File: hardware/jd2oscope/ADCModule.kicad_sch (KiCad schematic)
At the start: 2 parts, among them J1 5227161-2, U1 ADS7279IPW

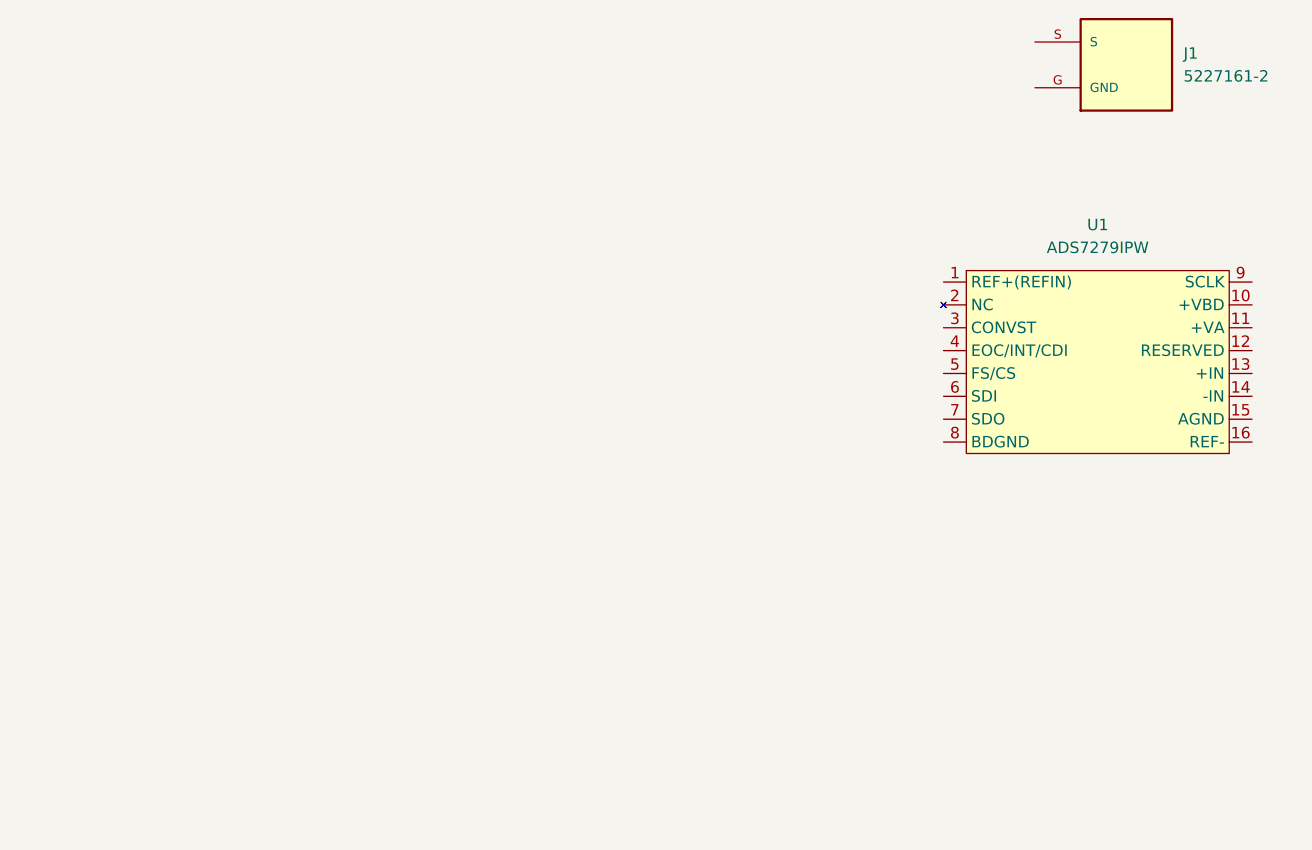
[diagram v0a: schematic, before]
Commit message: feat: opAmpCircuit cleanup
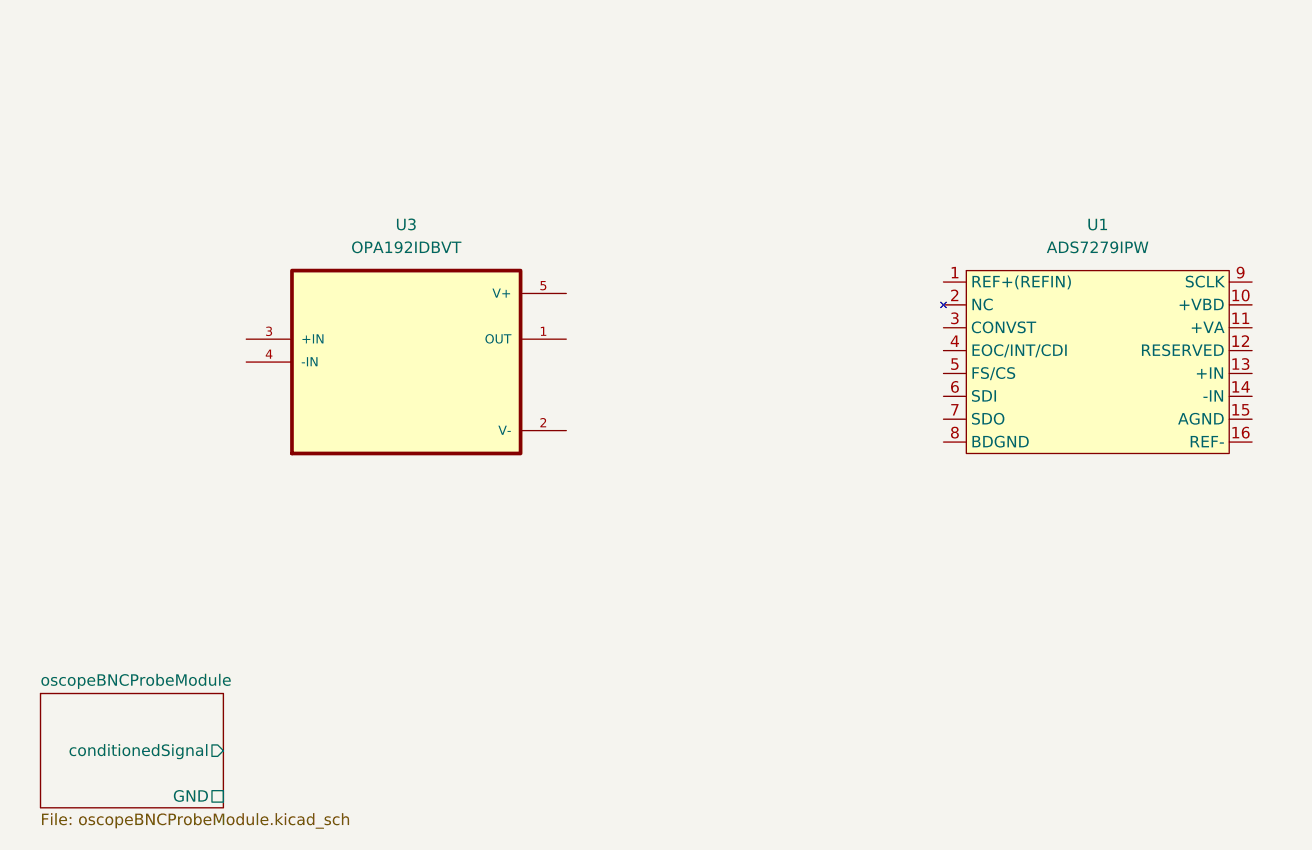
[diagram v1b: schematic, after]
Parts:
- removed J1: 5227161-2, 5227161-2:TE_5227161-2, symbol BNCFemaleConn:5227161-2
- added U3: OPA192IDBVT, OPA192IDBVT:SOT95P280X145-5N, symbol opAmp:OPA192IDBVT
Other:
- added sheet oscopeBNCProbeModule (oscopeBNCProbeModule.kicad_sch)
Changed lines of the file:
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@@
 	)
 	(symbol
-		(lib_id "BNCFemaleConn:5227161-2")
-		(at 158.75 59.69 0)
+		(lib_id "opAmp:OPA192IDBVT")
+		(at 78.74 92.71 0)
 		(unit 1)
 		(exclude_from_sim no)
@@
 		(dnp no)
 		(fields_autoplaced yes)
-		(property "Reference" "J1"
-			(at 165.1 58.4199 0)
-			(effects
-				(font
-					(size 1.27 1.27)
-				)
-				(justify left)
-			)
-		)
-		(property "Value" "5227161-2"
-			(at 165.1 60.9599 0)
-			(effects
-				(font
-					(size 1.27 1.27)
-				)
-				(justify left)
-			)
-		)
-		(property "Footprint" "5227161-2:TE_5227161-2"
-			(at 158.75 59.69 0)
+		(property "Reference" "U3"
+			(at 78.74 77.47 0)
+			(effects
+				(font
+					(size 1.27 1.27)
+				)
+			)
+		)
+		(property "Value" "OPA192IDBVT"
+			(at 78.74 80.01 0)
+			(effects
+				(font
+					(size 1.27 1.27)
+				)
+			)
+		)
+		(property "Footprint" "OPA192IDBVT:SOT95P280X145-5N"
+			(at 78.74 92.71 0)
 			(effects
 				(font
@@
 		)
 		(property "Datasheet" ""
-			(at 158.75 59.69 0)
+			(at 78.74 92.71 0)
 			(effects
 				(font
@@
 		)
 		(property "Description" ""
-			(at 158.75 59.69 0)
-			(effects
-				(font
-					(size 1.27 1.27)
-				)
-				(hide yes)
-			)
-		)
-		(property "Comment" "5227161-2"
-			(at 158.75 59.69 0)
-			(effects
-				(font
-					(size 1.27 1.27)
-				)
-				(justify bottom)
-				(hide yes)
-			)
-		)
-		(property "MF" "TE Connectivity"
-			(at 158.75 59.69 0)
-			(effects
-				(font
-					(size 1.27 1.27)
-				)
-				(justify bottom)
-				(hide yes)
-			)
-		)
-		(property "MAXIMUM_PACKAGE_HEIGHT" "16.13 mm"
-			(at 158.75 59.69 0)
-			(effects
-				(font
-					(size 1.27 1.27)
-				)
-				(justify bottom)
-				(hide yes)
-			)
-		)
-		(property "Package" "None"
-			(at 158.75 59.69 0)
+			(at 78.74 92.71 0)
+			(effects
+				(font
+					(size 1.27 1.27)
+				)
+				(hide yes)
+			)
+		)
+		(property "MF" "Texas Instruments"
+			(at 78.74 92.71 0)
+			(effects
+				(font
+					(size 1.27 1.27)
+				)
+				(justify bottom)
+				(hide yes)
+			)
+		)
+		(property "Description_1" "\n                        \n                            High-Voltage, Rail-to-Rail Input/Output, 5µV, 0.2µV/˚C, Precision Operational Amplifier\n                        \n"
+			(at 78.74 92.71 0)
+			(effects
+				(font
+					(size 1.27 1.27)
+				)
+				(justify bottom)
+				(hide yes)
+			)
+		)
+		(property "Package" "SOT-23-5 Texas Instruments"
+			(at 78.74 92.71 0)
 			(effects
 				(font
@@
 		)
 		(property "Price" "None"
-			(at 158.75 59.69 0)
-			(effects
-				(font
-					(size 1.27 1.27)
-				)
-				(justify bottom)
-				(hide yes)
-			)
-		)
-		(property "Check_prices" "https://www.snapeda.com/parts/5227161-2/TE+Connectivity/view-part/?ref=eda"
-			(at 158.75 59.69 0)
-			(effects
-				(font
-					(size 1.27 1.27)
-				)
-				(justify bottom)
-				(hide yes)
-			)
-		)
-		(property "STANDARD" "Manufacturer Recommendations"
-			(at 158.75 59.69 0)
-			(effects
-				(font
-					(size 1.27 1.27)
-				)
-				(justify bottom)
-				(hide yes)
-			)
-		)
-		(property "PARTREV" "B3"
-			(at 158.75 59.69 0)
-			(effects
-				(font
-					(size 1.27 1.27)
-				)
-				(justify bottom)
-				(hide yes)
-			)
-		)
-		(property "SnapEDA_Link" "https://www.snapeda.com/parts/5227161-2/TE+Connectivity/view-part/?ref=snap"
-			(at 158.75 59.69 0)
-			(effects
-				(font
-					(size 1.27 1.27)
-				)
-				(justify bottom)
-				(hide yes)
-			)
-		)
-		(property "MP" "5227161-2"
-			(at 158.75 59.69 0)
-			(effects
-				(font
-					(size 1.27 1.27)
-				)
-				(justify bottom)
-				(hide yes)
-			)
-		)
-		(property "EU_RoHS_Compliance" "Compliant with Exemptions"
-			(at 158.75 59.69 0)
-			(effects
-				(font
-					(size 1.27 1.27)
-				)
-				(justify bottom)
-				(hide yes)
-			)
-		)
-		(property "Description_1" "\n                        \n                            CONNECTOR, RF, BNC, JACK, PCB, RIGHT ANGLE, WITH PINS | TE Connectivity 5227161-2\n                        \n"
-			(at 158.75 59.69 0)
-			(effects
-				(font
-					(size 1.27 1.27)
-				)
-				(justify bottom)
-				(hide yes)
-			)
-		)
-		(property "Number_of_Positions" "1"
-			(at 158.75 59.69 0)
+			(at 78.74 92.71 0)
+			(effects
+				(font
+					(size 1.27 1.27)
+				)
+				(justify bottom)
+				(hide yes)
+			)
+		)
+		(property "SnapEDA_Link" "https://www.snapeda.com/parts/OPA192IDBVT/Texas+Instruments/view-part/?ref=snap"
+			(at 78.74 92.71 0)
+			(effects
+				(font
+					(size 1.27 1.27)
+				)
+				(justify bottom)
+				(hide yes)
+			)
+		)
+		(property "MP" "OPA192IDBVT"
+			(at 78.74 92.71 0)
 			(effects
 				(font
@@
 		)
 		(property "Availability" "In Stock"
-			(at 158.75 59.69 0)
-			(effects
-				(font
-					(size 1.27 1.27)
-				)
-				(justify bottom)
-				(hide yes)
-			)
-		)
-		(property "MANUFACTURER" "TE Connectivity"
-			(at 158.75 59.69 0)
-			(effects
-				(font
-					(size 1.27 1.27)
-				)
-				(justify bottom)
-				(hide yes)
-			)
-		)
-		(pin "S"
-		)
-		(pin "G"
+			(at 78.74 92.71 0)
+			(effects
+				(font
+					(size 1.27 1.27)
+				)
+				(justify bottom)
+				(hide yes)
+			)
+		)
+		(property "Check_prices" "https://www.snapeda.com/parts/OPA192IDBVT/Texas+Instruments/view-part/?ref=eda"
+			(at 78.74 92.71 0)
+			(effects
+				(font
+					(size 1.27 1.27)
+				)
+				(justify bottom)
+				(hide yes)
+			)
+		)
+		(pin "4"
+		)
+		(pin "5"
+		)
+		(pin "3"
+		)
+		(pin "2"
+		)
+		(pin "1"
+		)
+		(instances
+			(project ""
+				(path "/eb18a3da-9fbf-4329-a814-1afab785c817/a55cf82a-acda-4de6-8ce7-2cf91fdca590"
+					(reference "U3")
+					(unit 1)
+				)
+			)
+		)
+	)
+	(sheet
+		(at 38.1 129.54)
+		(size 20.32 12.7)
+		(fields_autoplaced yes)
+		(stroke
+			(width 0.1524)
+			(type solid)
+		)
+		(fill
+			(color 0 0 0 0.0000)
+		)
+		(property "Sheetname" "oscopeBNCProbeModule"
+			(at 38.1 128.8284 0)
+			(effects
+				(font
+					(size 1.27 1.27)
+				)
+				(justify left bottom)
+			)
+		)
+		(property "Sheetfile" "oscopeBNCProbeModule.kicad_sch"
+			(at 38.1 142.8246 0)
+			(effects
+				(font
+					(size 1.27 1.27)
+				)
+				(justify left top)
+			)
+		)
+		(pin "GND" passive
+			(at 58.42 140.97 0)
+			(effects
+				(font
+					(size 1.27 1.27)
+				)
+				(justify right)
+			)
+		)
+		(pin "conditionedSignal" output
+			(at 58.42 135.89 0)
+			(effects
+				(font
+					(size 1.27 1.27)
+				)
+				(justify right)
+			)
 		)
 		(instances
 			(project "jd2oscope"
 				(path "/eb18a3da-9fbf-4329-a814-1afab785c817/a55cf82a-acda-4de6-8ce7-2cf91fdca590"
-					(reference "J1")
-					(unit 1)
-				)
-			)
+					(page "2")
+				)
+			)

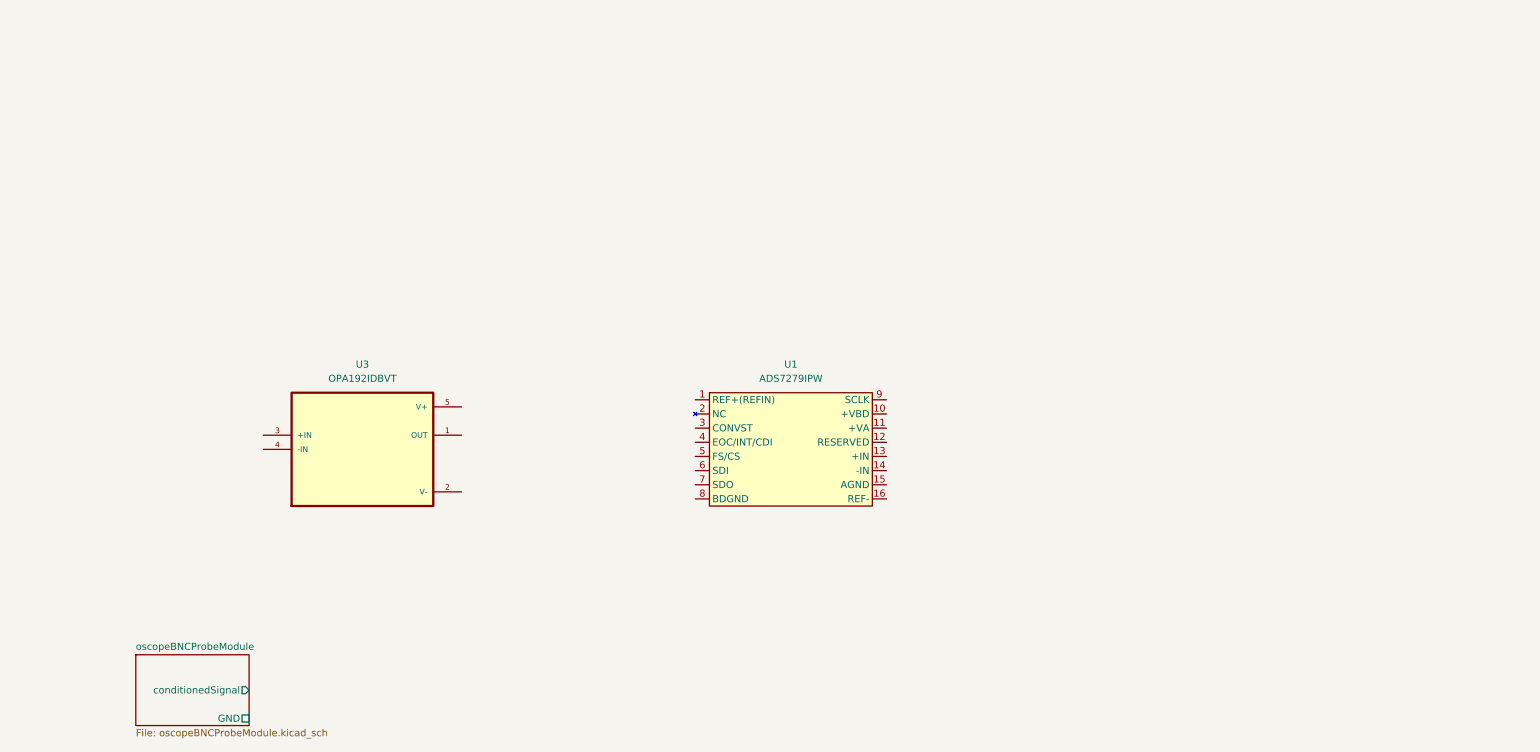
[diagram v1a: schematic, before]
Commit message: feat: screen implemented
alongside screen implementation, re-structured layout for schematics, and cleaned up SPI comm. conn.s; also implemented ADC module successfully (sans SPI section for it; that comes next)
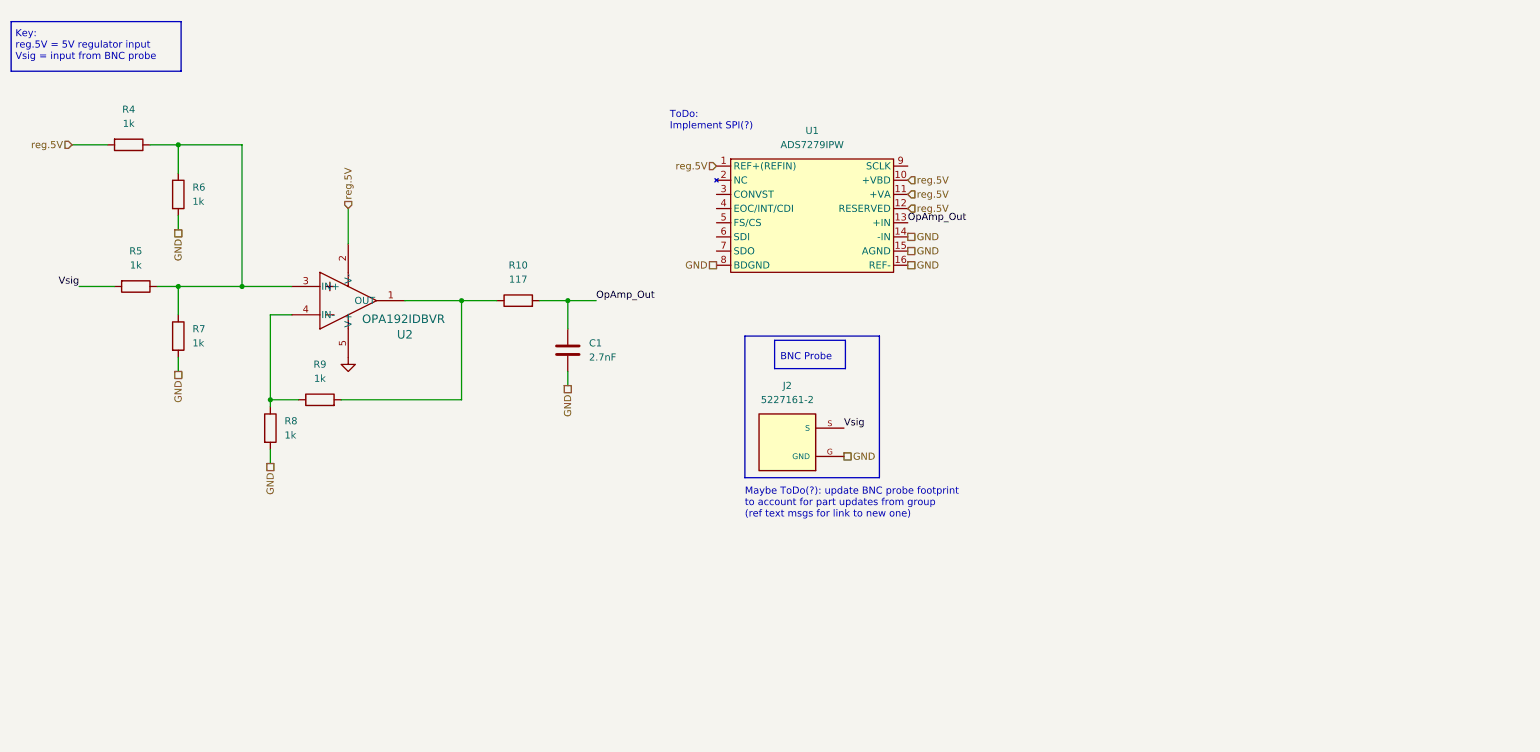
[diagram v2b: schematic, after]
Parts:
- removed U3: OPA192IDBVT, OPA192IDBVT:SOT95P280X145-5N, symbol opAmp:OPA192IDBVT
- added C1: 2.7nF, Capacitor_SMD:C_0603_1608Metric_Pad1.08x0.95mm_HandSolder, symbol Device:C
- added J2: 5227161-2, 5227161-2:TE_5227161-2, symbol BNCFemaleConn:5227161-2
- added R10: 117, Resistor_SMD:R_0603_1608Metric_Pad0.98x0.95mm_HandSolder, symbol Device:R
- added R4, R5, R6, R7, R8, R9: 1k, Resistor_SMD:R_0603_1608Metric_Pad0.98x0.95mm_HandSolder, symbol Device:R
- added U2: OPA192IDBVR, pot:SOT95P280X145-5N, symbol Op-amp:OPA192IDBVR
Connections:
- net reg.5V: now reaches U1.1 (REF+(REFIN))
- net reg.5V: now also U1.10 (+VBD), U1.11 (+VA), U1.12 (RESERVED), R4.2, U2.2 (V-)
- net OpAmp_Out: now reaches U1.13 (+IN)
- net OpAmp_Out: now also C1.1, R10.2
- net GND: now reaches U1.14 (-IN)
- net GND: now also U1.15 (AGND), U1.16 (REF-), U1.8 (BDGND), C1.2, J2.G (GND), R6.2, R7.2, R8.2, U2.5 (V+)
- new net: R8.1, R9.1, U2.4 (IN-)
- new net: R10.1, R9.2, U2.1 (OUT)
- new net: R4.1, R5.1, R6.1, R7.1, U2.3 (IN+)
- new net Vsig: J2.S, R5.2
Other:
- removed sheet oscopeBNCProbeModule
- note added: "BNC Probe"
- note added: "Key: reg.5V = 5V regulator input Vsig = input from BNC probe"
- note added: "Maybe ToDo(?): update BNC probe footprint to account for part updates from group (ref text msgs for link to new one)"
- note added: "ToDo: Implement SPI(?)"
- moved on the sheet: U1

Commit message: feat: lot of progress
added decoupling caps, implemented a lot more of the comm. protocol stuffs, updated BNC connector to updated version, added more notes for GPIO pin I/O for future code implementation, lot of other stuff too (frankly can't remember all of it lol); I commit here b/c want to back up progress b/4 I go get smth to eat ;)
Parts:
- removed J2: 5227161-2, 5227161-2:TE_5227161-2, symbol BNCFemaleConn:5227161-2
- added C10, C6, C7, C8, C9: 0.1u, symbol Device:C
- added J2: CONBNC001, CONBNC001:LINX_CONBNC001, symbol CONBNC001:CONBNC001
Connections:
- net GND: now also C10.2, C6.2, C7.2, C8.2, C9.2, J2.S1
- net Vsig: now also J2.1
- net reg.5V: now also C10.1, C6.1, C7.1, C8.1, C9.1
- net ADC_CONVST: now reaches U1.3 (CONVST)
- net ADC_EOC/INT: now reaches U1.4 (EOC/INT/CDI)
- net ADC_CS: now reaches U1.5 (FS/CS)
- net ADC_SDI: now reaches U1.6 (SDI)
- net ADC_SDO: now reaches U1.7 (SDO)
- net ADC_SCK: now reaches U1.9 (SCLK)
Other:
- note added: "EOC/INT: "End of Conversion/Interrupt"; signals when the ADC is done converting a signal (intended for use with an interrupt GPIO pin) CONVST: "Convert Start"; used to trigger a new conversion; best to drive this pin from a stable timer OR a PWM output from the ESP32 to achieve desired sampling rate (e.g., a sampling rate of 1 MSPS)"
- note added: "Note: 0.1uF = decoupling capacitors (they increase reliability/stability for power input pins; place as close as possible to the pin recieving the power!!)"
- note added: "Unique GPIO Pins to Consider/Implement: - ADC_EOC/INT (triggers when ADC finishes converting a signal) - ADC_CONVST (when triggered, starts converting a signal) - ADC_CS ("label" for the ADC for SPI; enables general SPI comm.s)"
- note added: "~59kHz lowpass (clarify that this is what we want(?))"
- note removed: "Maybe ToDo(?): update BNC probe footprint to account for part updates from group (ref text msgs for link to new one)"
- note removed: "ToDo: Implement SPI(?)"

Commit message: feat: more stuff added
yep
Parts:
- C1: value 2.7nF -> 2.7n
- C10, C6, C7, C8, C9: footprint (none) -> Capacitor_SMD:C_0603_1608Metric_Pad1.08x0.95mm_HandSolder

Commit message: feat: finished schematics
I think! Subject to change tho! for now though at least, I think they look clean asf hah~
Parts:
- renumbered C1 to C14, C9 to C15, C6 to C16, C7 to C18, C8 to C19, C10 to C6, R5 to R11, R6 to R12, R7 to R13, R8 to R14, R9 to R15, R10 to R16, R4 to R3, U2 to U6, U1 to U7
